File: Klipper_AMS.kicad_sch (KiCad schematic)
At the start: 12 parts, among them J1 VIN, U1 STM32F411CEUx, U2 TPS5430DDA

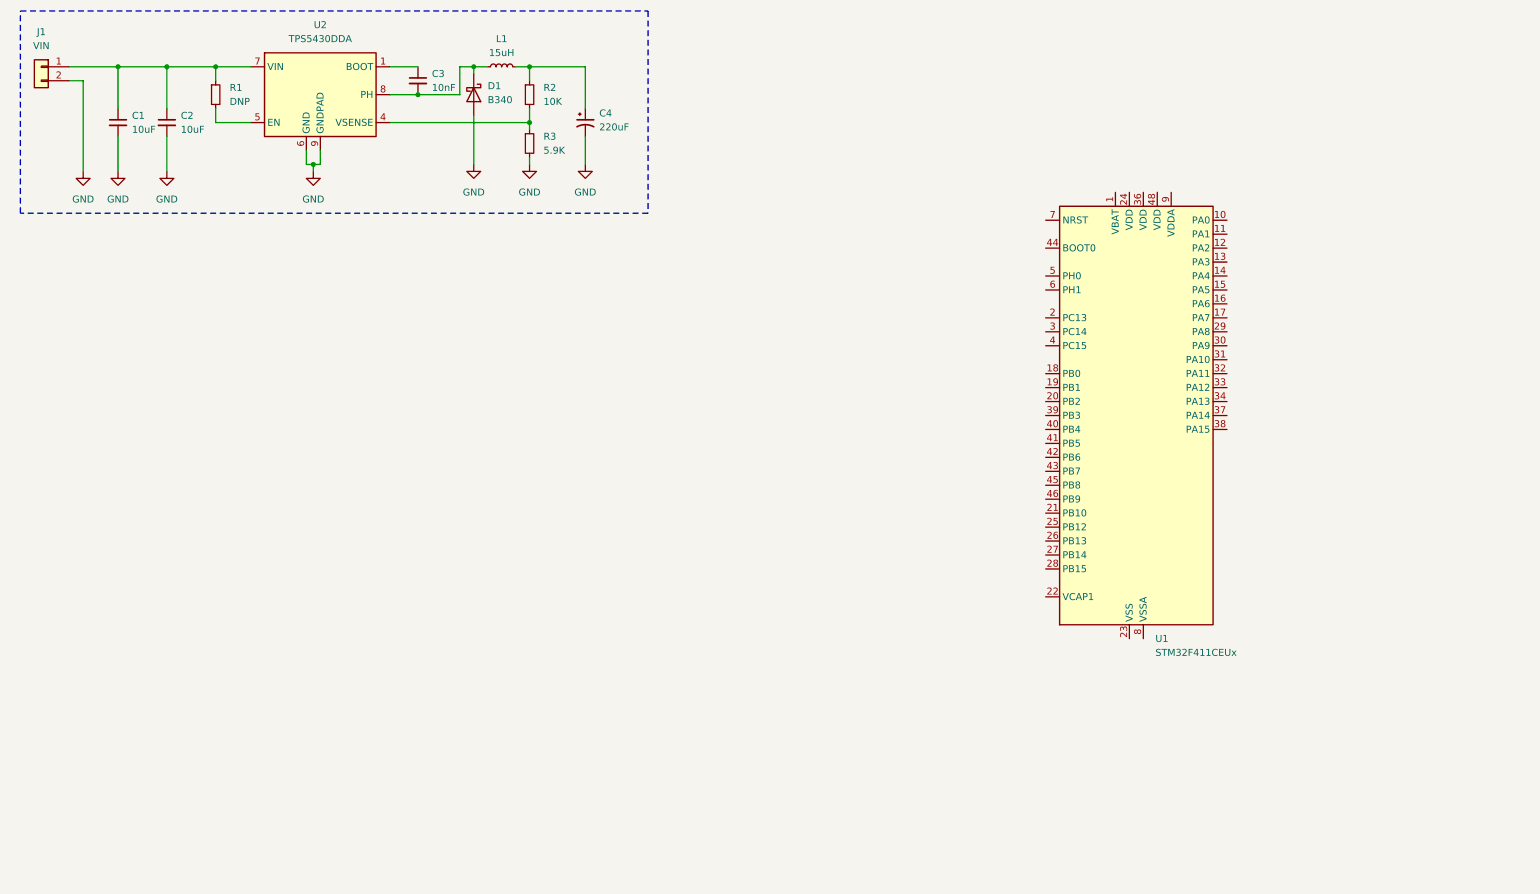
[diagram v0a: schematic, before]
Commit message: add motor driver
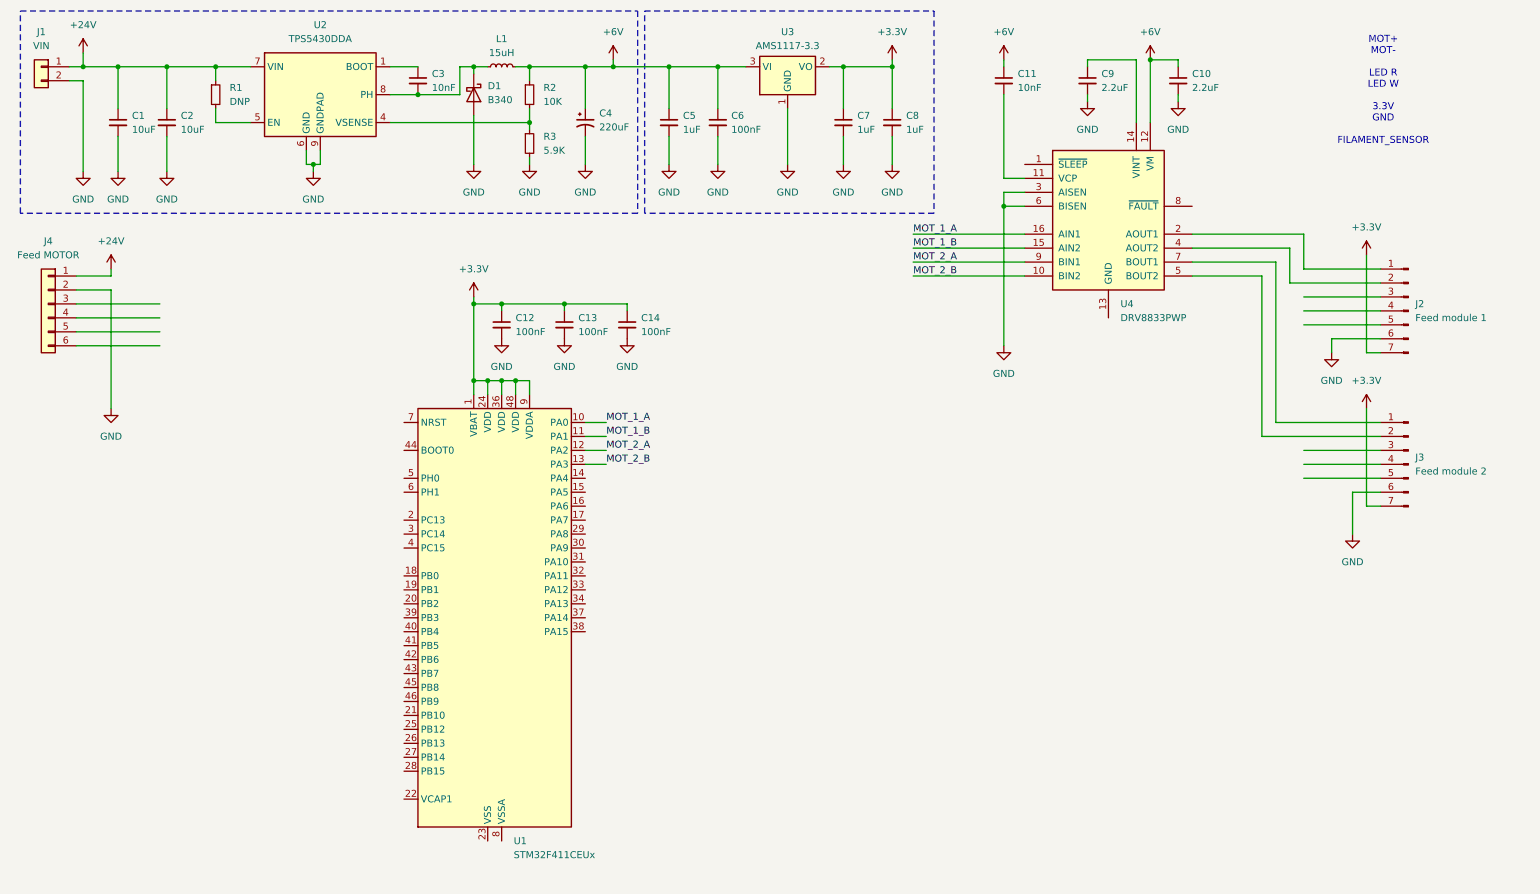
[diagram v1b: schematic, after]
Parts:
- added C10, C9: 2.2uF, symbol Device:C_Small
- added C11: 10nF, symbol Device:C_Small
- added C12, C13, C14, C6: 100nF, symbol Device:C_Small
- added C5, C7, C8: 1uF, symbol Device:C_Small
- added J2: Feed module 1, symbol Connector:Conn_01x07_Pin
- added J3: Feed module 2, symbol Connector:Conn_01x07_Pin
- added J4: Feed MOTOR, symbol Connector_Generic:Conn_01x06
- added U3: AMS1117-3.3, Package_TO_SOT_SMD:SOT-223-3_TabPin2, symbol Regulator_Linear:AMS1117-3.3
- added U4: DRV8833PWP, Package_SO:HTSSOP-16-1EP_4.4x5mm_P0.65mm_EP3.4x5mm_Mask2.46x2.31mm_ThermalVias, symbol Driver_Motor:DRV8833PWP
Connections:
- net GND: now also C10.2, C12.2, C13.2, C14.2, C5.2, C6.2, C7.2, C8.2, C9.2, J2.6 (Pin_6), J3.6 (Pin_6), J4.2 (Pin_2), U3.1 (GND), U4.3 (AISEN), U4.6 (BISEN)
- net +24V: now reaches C1.1, C2.1, J1.1 (Pin_1), R1.1, U2.7 (VIN)
- net +24V: now also J4.1 (Pin_1)
- net +6V: now reaches C4.1, L1.2, R2.1
- net +6V: now also C10.1, C11.1, C5.1, C6.1, U3.3 (VI), U4.12 (VM)
- net +3.3V: now reaches U1.1 (VBAT)
- net +3.3V: now also U1.24 (VDD), U1.36 (VDD), U1.48 (VDD), U1.9 (VDDA), C12.1, C13.1, C14.1, C7.1, C8.1, J2.7 (Pin_7), J3.7 (Pin_7), U3.2 (VO)
- net MOT_1_A: now reaches U1.10 (PA0)
- net MOT_1_A: now also U4.16 (AIN1)
- net MOT_1_B: now reaches U1.11 (PA1)
- net MOT_1_B: now also U4.15 (AIN2)
- net MOT_2_A: now reaches U1.12 (PA2)
- net MOT_2_A: now also U4.9 (BIN1)
- net MOT_2_B: now reaches U1.13 (PA3)
- net MOT_2_B: now also U4.10 (BIN2)
- new net: J3.1 (Pin_1), U4.7 (BOUT1)
- new net: J3.2 (Pin_2), U4.5 (BOUT2)
- new net: C11.2, U4.11 (VCP)
- new net: U4.13 (GND), U4.17 (GND)
- new net: C9.1, U4.14 (VINT)
- new net: J2.1 (Pin_1), U4.2 (AOUT1)
- new net: J2.2 (Pin_2), U4.4 (AOUT2)
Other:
- note added: "MOT+ MOT- LED R LED W 3.3V GND FILAMENT_SENSOR"
- moved on the sheet: U1

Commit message: add connector
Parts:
- removed C12, C13, C14: 100nF, symbol Device:C_Small
- removed J3: Feed module 2, symbol Connector:Conn_01x07_Pin
- removed U1: STM32F411CEUx, Package_DFN_QFN:QFN-48-1EP_7x7mm_P0.5mm_EP5.6x5.6mm, symbol MCU_ST_STM32F4:STM32F411CEUx
- added J3: Filament_Distance, symbol Connector_Generic:Conn_01x04
- added J5: HALL, symbol Connector_Generic:Conn_01x06
- added J6: RS485, symbol Connector_Generic:Conn_01x05
- added J7: DEBUG_SWDIO, symbol Connector_Generic:Conn_01x04
- added J8: DEBUG_UART, symbol Connector_Generic:Conn_01x04
- added U1: STM32F103C8Tx, Package_QFP:LQFP-48_7x7mm_P0.5mm, symbol MCU_ST_STM32F1:STM32F103C8Tx
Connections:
- net +3.3V: now also J3.1 (Pin_1), J5.2 (Pin_2); no longer J2.7 (Pin_7)
- net +6V: now also J2.6 (Pin_6)
- net GND: now also J2.7 (Pin_7), J3.4 (Pin_4), J5.1 (Pin_1); no longer J2.6 (Pin_6)
- new net: U1.23 (VSS), U1.35 (VSS), U1.47 (VSS)
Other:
- note added: "3.3V 150mA"
- note added: "6.5V 2A"
- note added: "ADC"
- note added: "IO"
- note added: "MOT+ MOT- FILAMENT_SENSOR LED W LED R 6.5V GND"
- note added: "x4"
- note removed: "MOT+ MOT- LED R LED W 3.3V GND FILAMENT_SENSOR"
